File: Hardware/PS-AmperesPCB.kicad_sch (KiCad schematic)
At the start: 8 parts, among them J1 PeripheralCAN, J2 PeripheralCAN

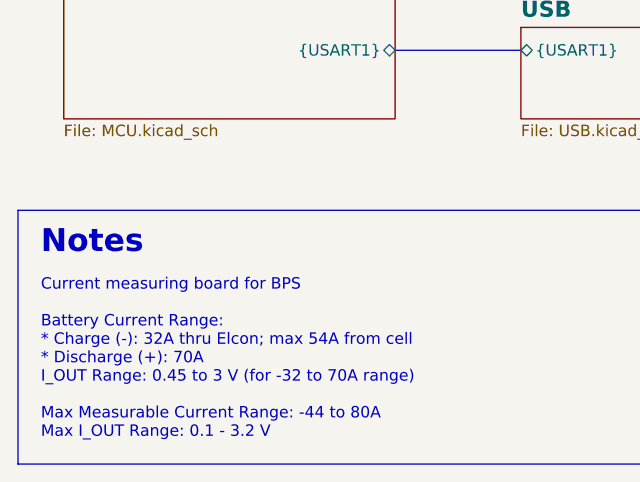
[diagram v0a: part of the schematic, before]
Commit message: renamed, added OR gate part
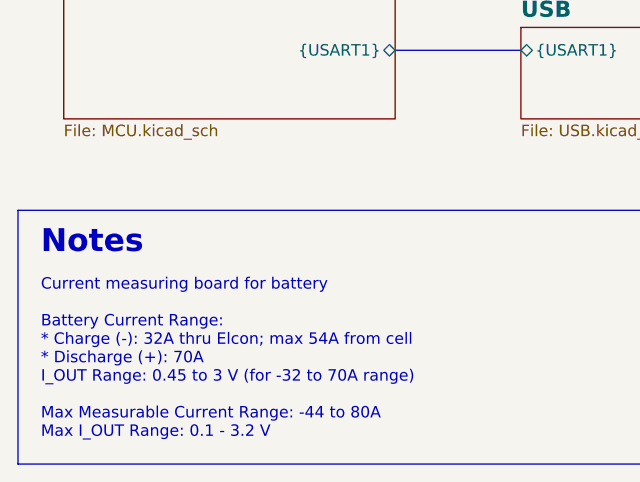
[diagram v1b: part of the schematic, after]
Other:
- note added: "Current measuring board for battery Battery Current Range: * Charge (-): 32A thru Elcon; max 54A from cell * Discharge (+): 70A I_OUT Range: 0.45 to 3 V (for -32 to 70A range) Max Measurable Current Range: -44 to 80A Max I_OUT Range: 0.1 - 3.2 V"
- note removed: "Current measuring board for BPS Battery Current Range: * Charge (-): 32A thru Elcon; max 54A from cell * Discharge (+): 70A I_OUT Range: 0.45 to 3 V (for -32 to 70A range) Max Measurable Current Range: -44 to 80A Max I_OUT Range: 0.1 - 3.2 V"
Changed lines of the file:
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@@
 		)
 	)
-	(text "Current measuring board for BPS\n\nBattery Current Range:\n* Charge (-): 32A thru Elcon; max 54A from cell\n* Discharge (+): 70A\nI_OUT Range: 0.45 to 3 V (for -32 to 70A range)\n\nMax Measurable Current Range: -44 to 80A\nMax I_OUT Range: 0.1 - 3.2 V\n"
+	(text "Current measuring board for battery\n\nBattery Current Range:\n* Charge (-): 32A thru Elcon; max 54A from cell\n* Discharge (+): 70A\nI_OUT Range: 0.45 to 3 V (for -32 to 70A range)\n\nMax Measurable Current Range: -44 to 80A\nMax I_OUT Range: 0.1 - 3.2 V\n"
 		(exclude_from_sim no)
 		(at 17.78 111.76 0)
@@
 		)
 		(instances
-			(project "BPS-AmperesPCB"
+			(project "PS-AmperesPCB"
 				(path "/a452d214-ea00-440d-a445-5d6103fda43a"
 					(page "4")
@@
 		)
 		(instances
-			(project "BPS-AmperesPCB"
+			(project "PS-AmperesPCB"
 				(path "/a452d214-ea00-440d-a445-5d6103fda43a"
 					(page "2")
@@
 		)
 		(instances
-			(project "BPS-AmperesPCB"
+			(project "PS-AmperesPCB"
 				(path "/a452d214-ea00-440d-a445-5d6103fda43a"
 					(page "6")
@@
 		)
 		(instances
-			(project "BPS-AmperesPCB"
+			(project "PS-AmperesPCB"
 				(path "/a452d214-ea00-440d-a445-5d6103fda43a"
 					(page "3")
@@
 		)
 		(instances
-			(project "BPS-AmperesPCB"
+			(project "PS-AmperesPCB"
 				(path "/a452d214-ea00-440d-a445-5d6103fda43a"
 					(page "5")

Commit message: lay out lay out
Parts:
- TP1: footprint (none) -> TestPoint:TestPoint_Pad_1.0x1.0mm
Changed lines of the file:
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@@
 		(lib_name "Logo_Placeholder_1")
 		(lib_id "utsvt-misc:Logo_Placeholder")
-		(at 120.65 72.39 0)
+		(at 121.92 72.39 0)
 		(unit 1)
 		(exclude_from_sim no)
@@
 		(fields_autoplaced yes)
 		(property "Reference" "LOGO1"
-			(at 120.65 68.58 0)
+			(at 121.92 68.58 0)
 			(effects
 				(font
@@
 		)
 		(property "Value" "logo placeholder"
-			(at 124.46 72.3899 0)
+			(at 125.73 72.3899 0)
 			(effects
 				(font
@@
 		)
 		(property "Footprint" "UTSVT_Logos:LHRs_LOGO"
-			(at 120.65 70.485 0)
+			(at 121.92 70.485 0)
 			(effects
 				(font
@@
 		)
 		(property "Datasheet" ""
-			(at 120.65 70.485 0)
+			(at 121.92 70.485 0)
 			(effects
 				(font
@@
 		)
 		(property "Description" "Graph footprint placeholder"
-			(at 120.65 72.39 0)
+			(at 121.92 72.39 0)
 			(effects
 				(font
@@
 		)
 		(property "PN" ""
-			(at 120.65 72.39 0)
+			(at 121.92 72.39 0)
 			(effects
 				(font
@@
 		)
 		(property "p/n" ""
-			(at 120.65 72.39 0)
+			(at 121.92 72.39 0)
 			(effects
 				(font
@@
 			)
 		)
-		(property "Footprint" ""
+		(property "Footprint" "TestPoint:TestPoint_Pad_1.0x1.0mm"
 			(at 66.04 40.64 0)
 			(effects

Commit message: more routing
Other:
- note added: "Current measuring board for battery Battery Current Range: * Charge (-): 32A thru Elcon; max 54A to cell * Discharge (+): 70A I_OUT Range: 0.45 - 3 V (for -32 to 70A range) Max Measurable Current Range: -44 to 80A with corresponding I_OUT Range: 0.1 - 3.2 V"
- note removed: "Current measuring board for battery Battery Current Range: * Charge (-): 32A thru Elcon; max 54A from cell * Discharge (+): 70A I_OUT Range: 0.45 to 3 V (for -32 to 70A range) Max Measurable Current Range: -44 to 80A Max I_OUT Range: 0.1 - 3.2 V"
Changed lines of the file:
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@@
 		)
 	)
-	(text "Current measuring board for battery\n\nBattery Current Range:\n* Charge (-): 32A thru Elcon; max 54A from cell\n* Discharge (+): 70A\nI_OUT Range: 0.45 to 3 V (for -32 to 70A range)\n\nMax Measurable Current Range: -44 to 80A\nMax I_OUT Range: 0.1 - 3.2 V\n"
+	(text "Current measuring board for battery\n\nBattery Current Range:\n* Charge (-): 32A thru Elcon; max 54A to cell\n* Discharge (+): 70A\nI_OUT Range: 0.45 - 3 V (for -32 to 70A range)\n\nMax Measurable Current Range: -44 to 80A\nwith corresponding I_OUT Range: 0.1 - 3.2 V\n"
 		(exclude_from_sim no)
 		(at 17.78 111.76 0)

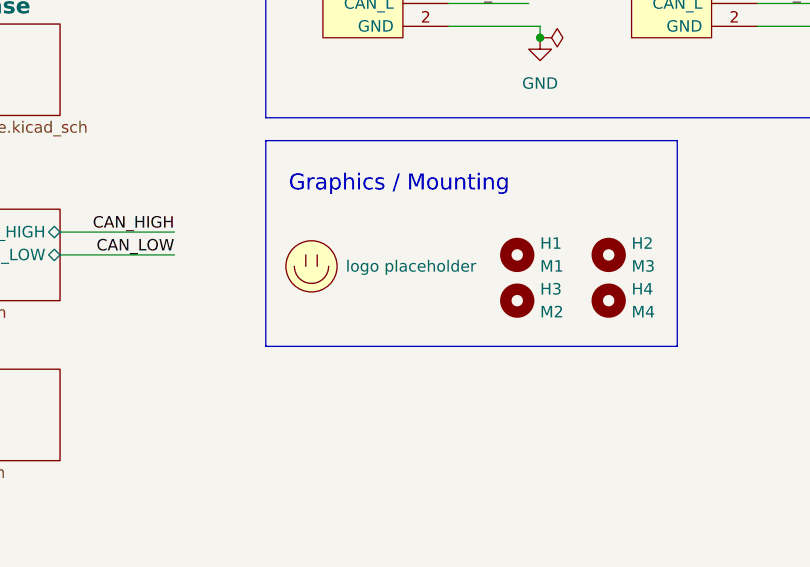
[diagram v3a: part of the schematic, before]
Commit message: more silkscreen, addressed some comments
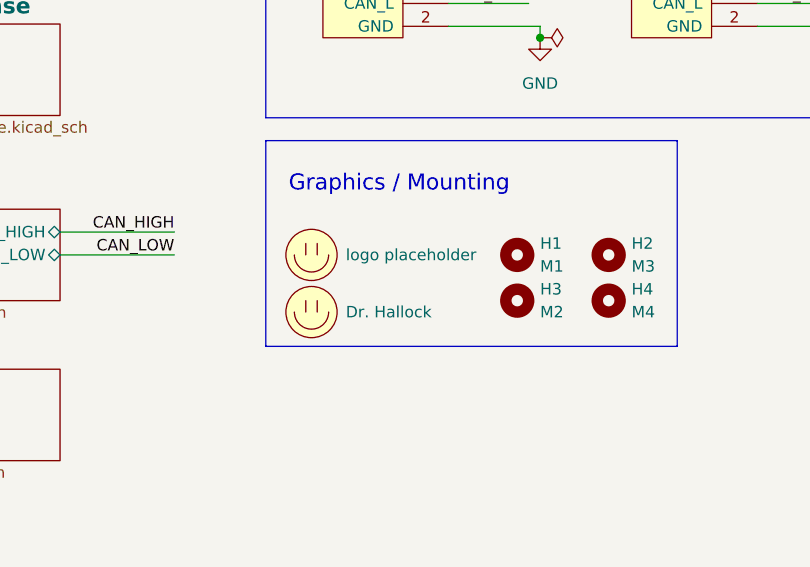
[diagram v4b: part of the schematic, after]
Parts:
- added LOGO2: Dr. Hallock, UTSVT_Logos:Hallock_Image_Tiny, symbol utsvt-misc:Logo_Placeholder
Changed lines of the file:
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@@
 		(lib_name "Logo_Placeholder_1")
 		(lib_id "utsvt-misc:Logo_Placeholder")
-		(at 121.92 72.39 0)
+		(at 121.92 71.12 0)
 		(unit 1)
 		(exclude_from_sim no)
@@
 		(fields_autoplaced yes)
 		(property "Reference" "LOGO1"
-			(at 121.92 68.58 0)
+			(at 121.92 67.31 0)
 			(effects
 				(font
@@
 		)
 		(property "Value" "logo placeholder"
-			(at 125.73 72.3899 0)
+			(at 125.73 71.1199 0)
 			(effects
 				(font
@@
 		)
 		(property "Footprint" "UTSVT_Logos:LHRs_LOGO"
-			(at 121.92 70.485 0)
+			(at 121.92 69.215 0)
 			(effects
 				(font
@@
 		)
 		(property "Datasheet" ""
-			(at 121.92 70.485 0)
+			(at 121.92 69.215 0)
 			(effects
 				(font
@@
 		)
 		(property "Description" "Graph footprint placeholder"
-			(at 121.92 72.39 0)
+			(at 121.92 71.12 0)
 			(effects
 				(font
@@
 		)
 		(property "PN" ""
-			(at 121.92 72.39 0)
+			(at 121.92 71.12 0)
 			(effects
 				(font
@@
 		)
 		(property "p/n" ""
-			(at 121.92 72.39 0)
+			(at 121.92 71.12 0)
 			(effects
 				(font
@@
 					(unit 1)
 				)
+			)
+		)
+	)
+	(symbol
+		(lib_id "utsvt-misc:Logo_Placeholder")
+		(at 121.92 77.47 0)
+		(unit 1)
+		(exclude_from_sim no)
+		(in_bom yes)
+		(on_board yes)
+		(dnp no)
+		(fields_autoplaced yes)
+		(property "Reference" "LOGO2"
+			(at 121.92 73.66 0)
+			(effects
+				(font
+					(size 1.27 1.27)
+				)
+				(hide yes)
+			)
+		)
+		(property "Value" "Dr. Hallock"
+			(at 125.73 77.4699 0)
+			(effects
+				(font
+					(size 1.27 1.27)
+				)
+				(justify left)
+			)
+		)
+		(property "Footprint" "UTSVT_Logos:Hallock_Image_Tiny"
+			(at 121.92 75.565 0)
+			(effects
+				(font
+					(size 1.27 1.27)
+				)
+				(hide yes)
+			)
+		)
+		(property "Datasheet" ""
+			(at 121.92 75.565 0)
+			(effects
+				(font
+					(size 1.27 1.27)
+				)
+				(hide yes)
+			)
+		)
+		(property "Description" "Graph footprint placeholder"
+			(at 121.92 77.47 0)
+			(effects
+				(font
+					(size 1.27 1.27)
+				)
+				(hide yes)
+			)
+		)
+		(property "PN" ""
+			(at 121.92 77.47 0)
+			(effects
+				(font
+					(size 1.27 1.27)
+				)
+				(hide yes)
+			)
+		)
+		(property "p/n" ""
+			(at 121.92 77.47 0)
+			(effects
+				(font
+					(size 1.27 1.27)
+				)
+				(hide yes)
+			)
+		)
+		(instances
+			(project ""
+				(path "/a452d214-ea00-440d-a445-5d6103fda43a"
+					(reference "LOGO2")
+					(unit 1)
+				)

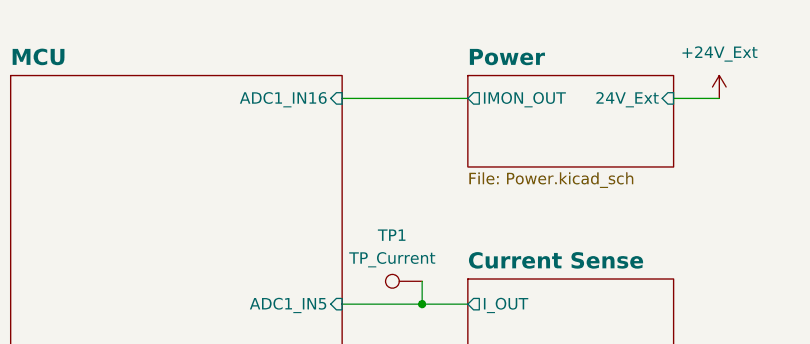
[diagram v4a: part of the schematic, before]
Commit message: new dpdt switch, layout done
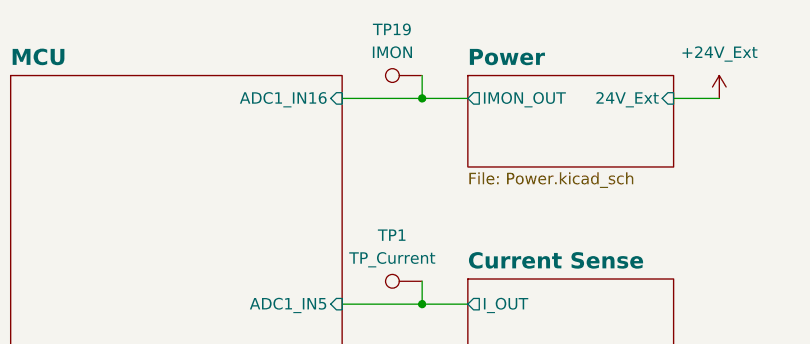
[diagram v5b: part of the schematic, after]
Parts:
- added TP19: IMON, TestPoint:TestPoint_Keystone_5005-5009_Compact, symbol Connector:TestPoint
- TP1: footprint TestPoint:TestPoint_Pad_1.0x1.0mm -> TestPoint:TestPoint_Keystone_5005-5009_Compact
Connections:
- net MCU/ADC1_IN16: now also TP19.1
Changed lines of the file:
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@@
 		(color 0 0 0 0)
 	)
+	(junction
+		(at 66.04 25.4)
+		(diameter 0)
+		(color 0 0 0 0)
+	)
 	(wire
 		(pts
@@
 	(wire
 		(pts
+			(xy 66.04 25.4) (xy 71.12 25.4)
+		)
+		(stroke
+			(width 0)
+			(type default)
+		)
+	)
+	(wire
+		(pts
 			(xy 181.61 36.83) (xy 181.61 38.1)
 		)
@@
 	(wire
 		(pts
+			(xy 66.04 22.86) (xy 66.04 25.4)
+		)
+		(stroke
+			(width 0)
+			(type default)
+		)
+	)
+	(wire
+		(pts
 			(xy 93.98 71.12) (xy 106.68 71.12)
 		)
@@
 	(wire
 		(pts
-			(xy 57.15 25.4) (xy 71.12 25.4)
+			(xy 57.15 25.4) (xy 66.04 25.4)
 		)
 		(stroke
@@
 	)
 	(symbol
+		(lib_id "Connector:TestPoint")
+		(at 66.04 22.86 90)
+		(unit 1)
+		(exclude_from_sim no)
+		(in_bom yes)
+		(on_board yes)
+		(dnp no)
+		(fields_autoplaced yes)
+		(property "Reference" "TP19"
+			(at 62.738 17.78 90)
+			(effects
+				(font
+					(size 1.27 1.27)
+				)
+			)
+		)
+		(property "Value" "IMON"
+			(at 62.738 20.32 90)
+			(effects
+				(font
+					(size 1.27 1.27)
+				)
+			)
+		)
+		(property "Footprint" "TestPoint:TestPoint_Keystone_5005-5009_Compact"
+			(at 66.04 17.78 0)
+			(effects
+				(font
+					(size 1.27 1.27)
+				)
+				(hide yes)
+			)
+		)
+		(property "Datasheet" "~"
+			(at 66.04 17.78 0)
+			(effects
+				(font
+					(size 1.27 1.27)
+				)
+				(hide yes)
+			)
+		)
+		(property "Description" "test point"
+			(at 66.04 22.86 0)
+			(effects
+				(font
+					(size 1.27 1.27)
+				)
+				(hide yes)
+			)
+		)
+		(pin "1"
+		)
+		(instances
+			(project "PS-AmperesPCB"
+				(path "/a452d214-ea00-440d-a445-5d6103fda43a"
+					(reference "TP19")
+					(unit 1)
+				)
+			)
+		)
+	)
+	(symbol
 		(lib_id "utsvt-connectors:PeripheralCANConnector")
 		(at 161.29 41.91 0)
@@
 			)
 		)
-		(property "Footprint" "TestPoint:TestPoint_Pad_1.0x1.0mm"
+		(property "Footprint" "TestPoint:TestPoint_Keystone_5005-5009_Compact"
 			(at 66.04 40.64 0)
 			(effects
